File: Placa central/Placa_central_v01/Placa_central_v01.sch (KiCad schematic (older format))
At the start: 35 parts, among them SW1 SW_comando1

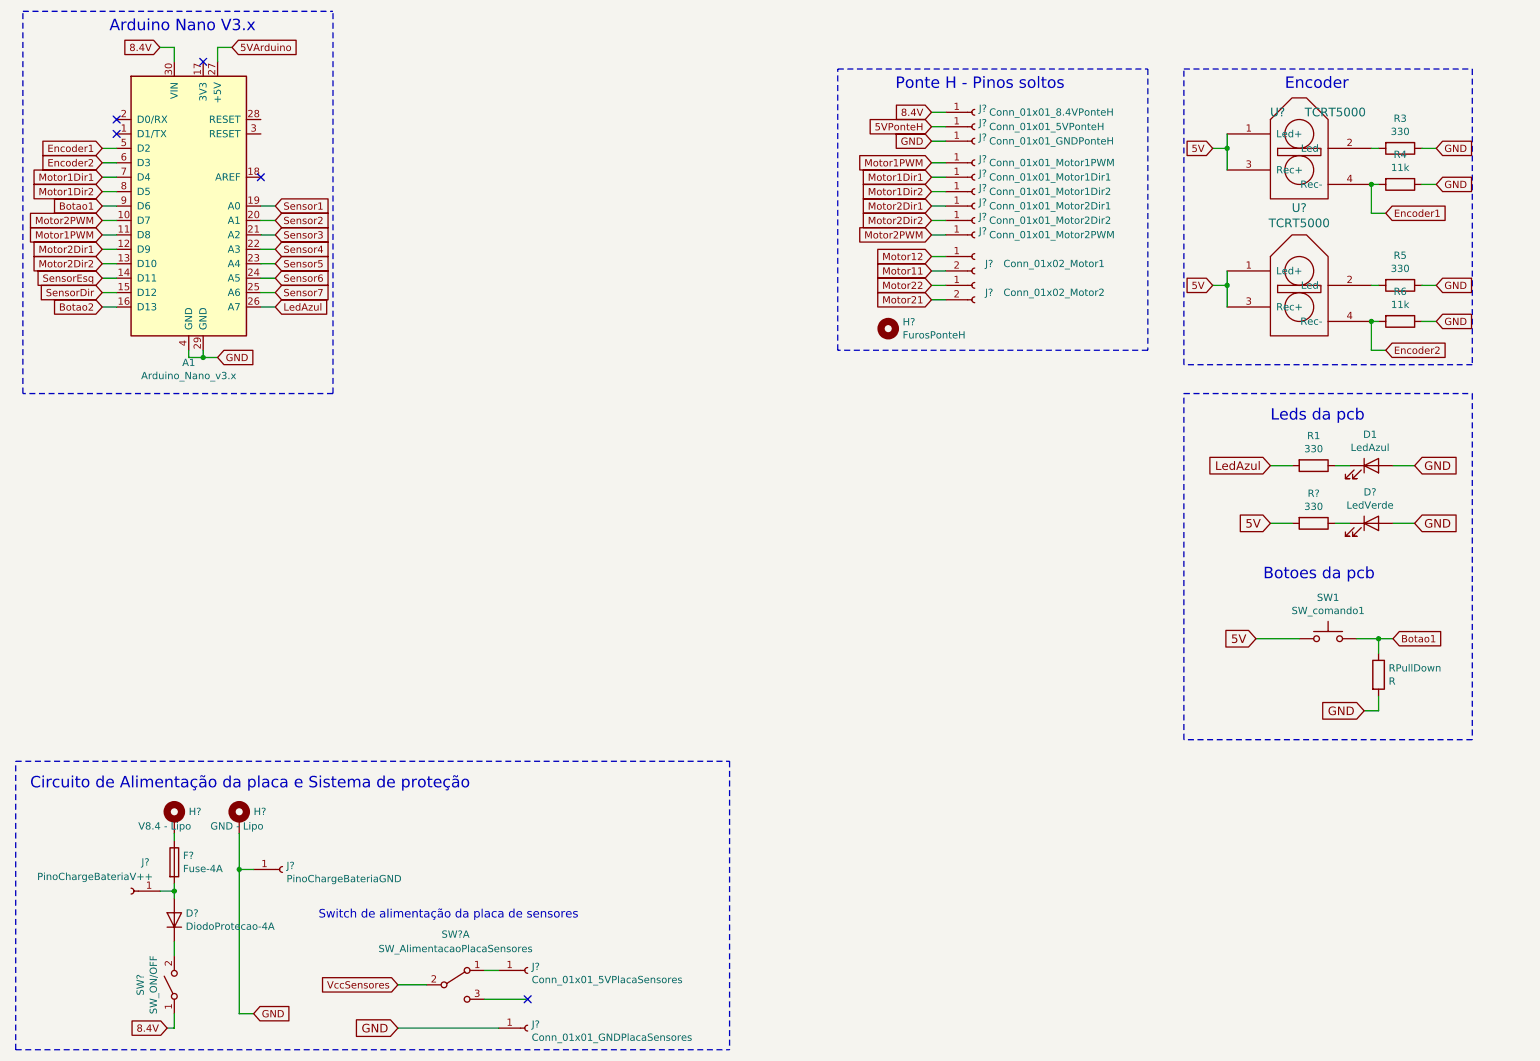
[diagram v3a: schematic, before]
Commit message: Terminado o esquemático do circuito
Feito: circuito medidor de bateria; pads do arduino; pads do encoder; pads da ponte H; pads da placa de sensores;
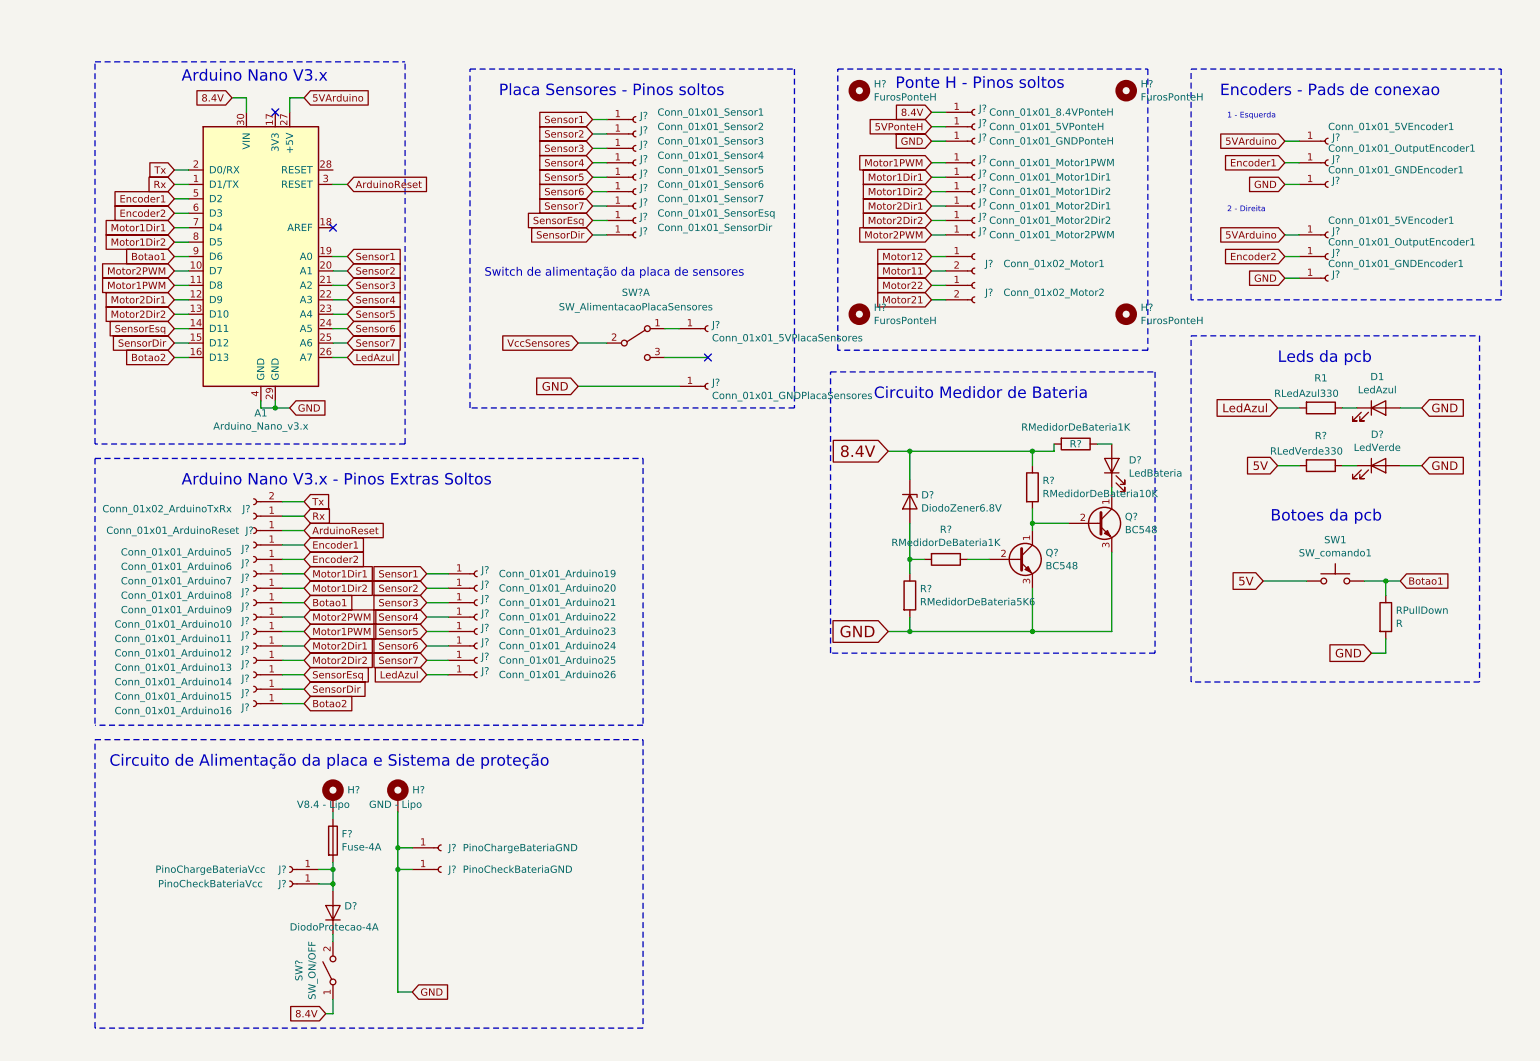
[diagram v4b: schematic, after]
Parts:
- removed R3, R5: 330, symbol Device:R
- removed R4, R6: 11k, symbol Device:R
- removed U? (x2): TCRT5000, symbol Sensores_e_componentes_SL:TCRT5000
- added D?: DiodoZener6.8V, symbol Device:D_Zener
- added D?: LedBateria, symbol Device:LED
- added H? (x3): FurosPonteH, symbol Mechanical:MountingHole
- added J? (x2): Conn_01x01_5VEncoder1, symbol Connector:Conn_01x01_Female
- added J? (x2): Conn_01x01_OutputEncoder1, symbol Connector:Conn_01x01_Female
- added J? (x2): Conn_01x01_GNDEncoder1, symbol Connector:Conn_01x01_Female
- added J?: Conn_01x01_Sensor1, symbol Connector:Conn_01x01_Female
- added J?: Conn_01x01_Sensor2, symbol Connector:Conn_01x01_Female
- added J?: Conn_01x01_Sensor3, symbol Connector:Conn_01x01_Female
- added J?: Conn_01x01_Sensor4, symbol Connector:Conn_01x01_Female
- added J?: Conn_01x01_Sensor5, symbol Connector:Conn_01x01_Female
- added J?: Conn_01x01_Sensor6, symbol Connector:Conn_01x01_Female
- added J?: Conn_01x01_Sensor7, symbol Connector:Conn_01x01_Female
- added J?: Conn_01x01_SensorEsq, symbol Connector:Conn_01x01_Female
- added J?: Conn_01x01_SensorDir, symbol Connector:Conn_01x01_Female
- added J?: PinoCheckBateriaGND, symbol Connector:Conn_01x01_Female
- added J?: PinoCheckBateriaVcc, symbol Connector:Conn_01x01_Female
- added J?: Conn_01x01_Arduino16, symbol Connector:Conn_01x01_Female
- added J?: Conn_01x01_Arduino15, symbol Connector:Conn_01x01_Female
- added J?: Conn_01x01_Arduino14, symbol Connector:Conn_01x01_Female
- added J?: Conn_01x01_Arduino13, symbol Connector:Conn_01x01_Female
- added J?: Conn_01x01_Arduino12, symbol Connector:Conn_01x01_Female
- added J?: Conn_01x01_Arduino11, symbol Connector:Conn_01x01_Female
- added J?: Conn_01x01_Arduino10, symbol Connector:Conn_01x01_Female
- added J?: Conn_01x01_Arduino9, symbol Connector:Conn_01x01_Female
- added J?: Conn_01x01_Arduino8, symbol Connector:Conn_01x01_Female
- added J?: Conn_01x01_Arduino7, symbol Connector:Conn_01x01_Female
- added J?: Conn_01x01_Arduino6, symbol Connector:Conn_01x01_Female
- added J?: Conn_01x01_Arduino5, symbol Connector:Conn_01x01_Female
- added J?: Conn_01x01_Arduino26, symbol Connector:Conn_01x01_Female
- added J?: Conn_01x01_Arduino25, symbol Connector:Conn_01x01_Female
- added J?: Conn_01x01_Arduino24, symbol Connector:Conn_01x01_Female
- added J?: Conn_01x01_Arduino23, symbol Connector:Conn_01x01_Female
- added J?: Conn_01x01_Arduino22, symbol Connector:Conn_01x01_Female
- added J?: Conn_01x01_Arduino21, symbol Connector:Conn_01x01_Female
- added J?: Conn_01x01_Arduino20, symbol Connector:Conn_01x01_Female
- added J?: Conn_01x01_Arduino19, symbol Connector:Conn_01x01_Female
- added J?: Conn_01x02_ArduinoTxRx, symbol Connector:Conn_01x02_Female
- added J?: Conn_01x01_ArduinoReset, symbol Connector:Conn_01x01_Female
- added Q? (x2): BC548, Package_TO_SOT_THT:TO-92_Inline, symbol Transistor_BJT:BC548
- added R? (x2): RMedidorDeBateria1K, symbol Device:R
- added R?: RMedidorDeBateria5K6, symbol Device:R
- added R?: RMedidorDeBateria10K, symbol Device:R
- J?: value PinoChargeBateriaV++ -> PinoChargeBateriaVcc
- R1: value 330 -> RLedAzul330
- R?: value 330 -> RLedVerde330
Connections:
- net 5VArduino: now also J?.1 (Pin_1), J?.1 (Pin_1)
- net 8.4V: now also D?.1 (K), R?.1, R?.2
- net Botao1: now also J?.1 (Pin_1)
- net Botao2: now also J?.1 (Pin_1)
- net Encoder1: now also J?.1 (Pin_1), J?.1 (Pin_1)
- net Encoder2: now also J?.1 (Pin_1), J?.1 (Pin_1)
- net GND: now also J?.1 (Pin_1), J?.1 (Pin_1), J?.1 (Pin_1), Q?.3 (E), Q?.3 (E), R?.2
- net LedAzul: now also J?.1 (Pin_1)
- net Motor1Dir1: now also J?.1 (Pin_1)
- net Motor1Dir2: now also J?.1 (Pin_1)
- net Motor1PWM: now also J?.1 (Pin_1)
- net Motor2Dir1: now also J?.1 (Pin_1)
- net Motor2Dir2: now also J?.1 (Pin_1)
- net Motor2PWM: now also J?.1 (Pin_1)
- net Sensor1: now also J?.1 (Pin_1), J?.1 (Pin_1)
- net Sensor2: now also J?.1 (Pin_1), J?.1 (Pin_1)
- net Sensor3: now also J?.1 (Pin_1), J?.1 (Pin_1)
- net Sensor4: now also J?.1 (Pin_1), J?.1 (Pin_1)
- net Sensor5: now also J?.1 (Pin_1), J?.1 (Pin_1)
- net Sensor6: now also J?.1 (Pin_1), J?.1 (Pin_1)
- net Sensor7: now also J?.1 (Pin_1), J?.1 (Pin_1)
- net SensorDir: now also J?.1 (Pin_1), J?.1 (Pin_1)
- net SensorEsq: now also J?.1 (Pin_1), J?.1 (Pin_1)
- net Rx: now reaches A1.1 (D1/TX)
- net Rx: now also J?.1 (Pin_1)
- net Tx: now reaches A1.2 (D0/RX)
- net Tx: now also J?.2 (Pin_2)
- net ArduinoReset: now reaches A1.3 (RESET)
- net ArduinoReset: now also J?.1 (Pin_1)
- net at D?.2 (A), F?.2, J?.1 (Pin_1): now also J?.1 (Pin_1)
- new net: D?.2 (A), R?.1, R?.2
- new net: Q?.2 (B), R?.1
- new net: Q?.1 (C), Q?.2 (B), R?.2
- new net: D?.2 (A), R?.1
- new net: D?.1 (K), Q?.1 (C)
- no-connect marks 5 -> 3
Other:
- note added: "1 - Esquerda\n"
- note added: "2 - Direita"
- note added: "Arduino Nano V3.x - Pinos Extras Soltos"
- note added: "Circuito Medidor de Bateria"
- note added: "Encoders - Pads de conexao"
- note added: "Placa Sensores - Pinos soltos"
- note removed: "Encoder"
- moved on the sheet: A1, D1, D?, F?, H?, J?, R1, R?, RPullDown, SW1, SW?, SW?A

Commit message: Acertada nomeclatura do encoder
De encoder1 para encoderEsq e a mesma coisa pro outro.
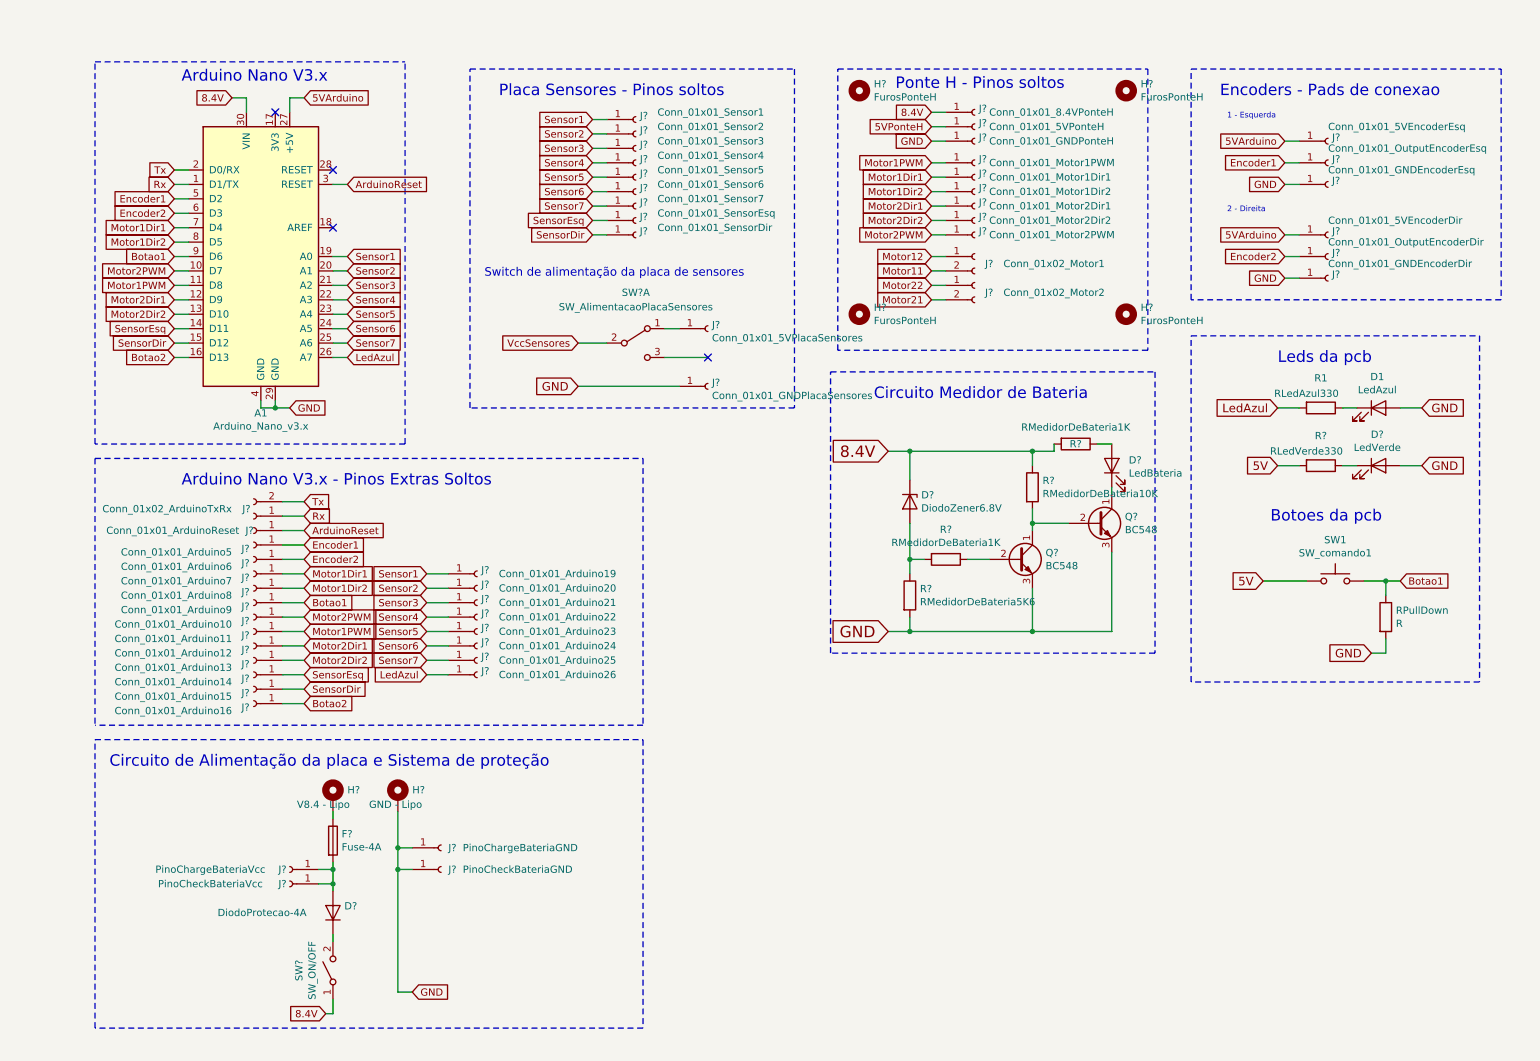
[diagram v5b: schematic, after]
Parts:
- J?: value Conn_01x01_5VEncoder1 -> Conn_01x01_5VEncoderEsq
- J?: value Conn_01x01_OutputEncoder1 -> Conn_01x01_OutputEncoderEsq
- J?: value Conn_01x01_GNDEncoder1 -> Conn_01x01_GNDEncoderEsq
- J?: value Conn_01x01_5VEncoder1 -> Conn_01x01_5VEncoderDir
- J?: value Conn_01x01_OutputEncoder1 -> Conn_01x01_OutputEncoderDir
- J?: value Conn_01x01_GNDEncoder1 -> Conn_01x01_GNDEncoderDir
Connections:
- no-connect marks 3 -> 4
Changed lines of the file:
@@
 P 2750 6800
 F 0 "D?" V 2796 6721 50  0000 R CNN
-F 1 "DiodoProtecao-4A" V 2650 7100 50  0000 R CNN
+F 1 "DiodoProtecao-4A" V 2750 7600 50  0000 R CNN
 F 2 "" H 2750 6800 50  0001 C CNN
 F 3 "~" H 2750 6800 50  0001 C CNN
@@
 P 9650 1450
 F 0 "J?" H 9678 1476 50  0000 L CNN
-F 1 "Conn_01x01_5VEncoder1" H 9650 1550 50  0000 L CNN
+F 1 "Conn_01x01_5VEncoderEsq" H 9650 1550 50  0000 L CNN
 F 2 "" H 9650 1450 50  0001 C CNN
 F 3 "~" H 9650 1450 50  0001 C CNN
@@
 P 9650 1600
 F 0 "J?" H 9678 1626 50  0000 L CNN
-F 1 "Conn_01x01_OutputEncoder1" H 9650 1700 50  0000 L CNN
+F 1 "Conn_01x01_OutputEncoderEsq" H 9650 1700 50  0000 L CNN
 F 2 "" H 9650 1600 50  0001 C CNN
 F 3 "~" H 9650 1600 50  0001 C CNN
@@
 P 9650 1750
 F 0 "J?" H 9677 1776 50  0000 L CNN
-F 1 "Conn_01x01_GNDEncoder1" H 9650 1850 50  0000 L CNN
+F 1 "Conn_01x01_GNDEncoderEsq" H 9650 1850 50  0000 L CNN
 F 2 "" H 9650 1750 50  0001 C CNN
 F 3 "~" H 9650 1750 50  0001 C CNN
@@
 P 9650 2100
 F 0 "J?" H 9678 2126 50  0000 L CNN
-F 1 "Conn_01x01_5VEncoder1" H 9650 2200 50  0000 L CNN
+F 1 "Conn_01x01_5VEncoderDir" H 9650 2200 50  0000 L CNN
 F 2 "" H 9650 2100 50  0001 C CNN
 F 3 "~" H 9650 2100 50  0001 C CNN
@@
 P 9650 2250
 F 0 "J?" H 9678 2276 50  0000 L CNN
-F 1 "Conn_01x01_OutputEncoder1" H 9650 2350 50  0000 L CNN
+F 1 "Conn_01x01_OutputEncoderDir" H 9650 2350 50  0000 L CNN
 F 2 "" H 9650 2250 50  0001 C CNN
 F 3 "~" H 9650 2250 50  0001 C CNN
@@
 P 9650 2400
 F 0 "J?" H 9677 2426 50  0000 L CNN
-F 1 "Conn_01x01_GNDEncoder1" H 9650 2500 50  0000 L CNN
+F 1 "Conn_01x01_GNDEncoderDir" H 9650 2500 50  0000 L CNN
 F 2 "" H 9650 2400 50  0001 C CNN
 F 3 "~" H 9650 2400 50  0001 C CNN
@@
 Wire Wire Line
 	2550 4150 2400 4150
+NoConn ~ 2750 1650
 $EndSCHEMATC

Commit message: Pequenas mudanças
Acertado nomeclatura de resistor; colocado um resistor no circuito de medição na tensão da bateria (separado do circuito de charga da bateria); gerado a lista de componentes (.csv)
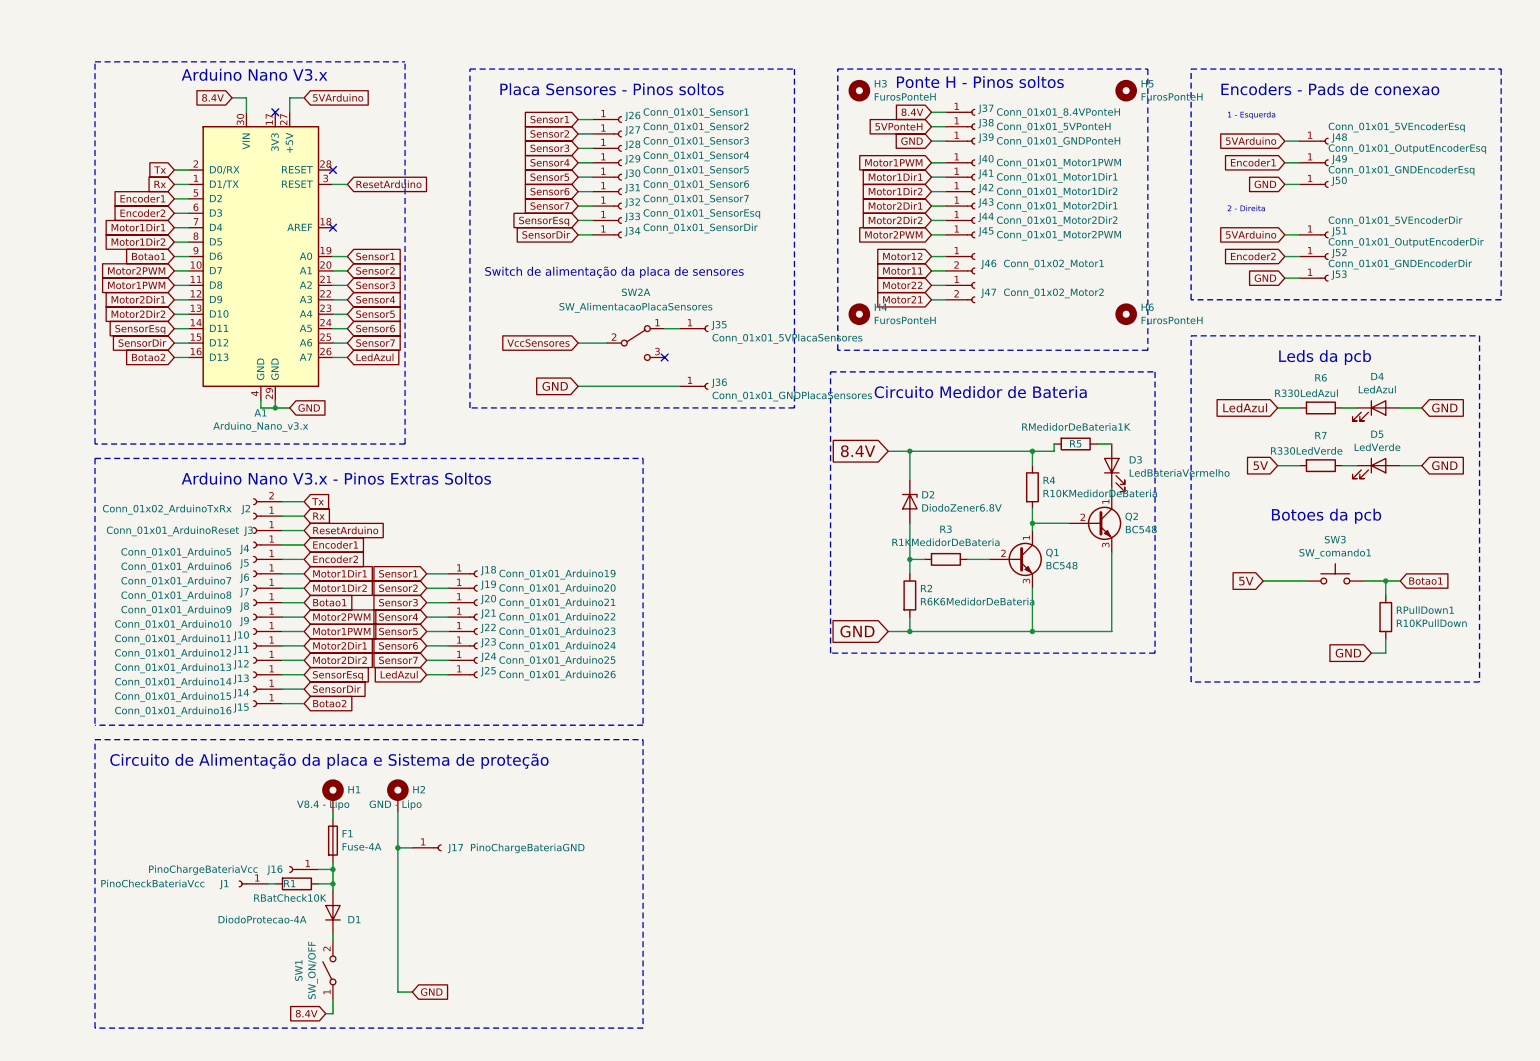
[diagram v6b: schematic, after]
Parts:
- removed J?: PinoCheckBateriaGND, symbol Connector:Conn_01x01_Female
- added R1: RBatCheck10K, symbol Device:R
- D3: renamed from D?; value LedBateria -> LedBateriaVermelho
- R2: renamed from R?; value RMedidorDeBateria5K6 -> R6K6MedidorDeBateria
- R3: renamed from R?; value RMedidorDeBateria1K -> R1KMedidorDeBateria
- R4: renamed from R?; value RMedidorDeBateria10K -> R10KMedidorDeBateria
- R6: renamed from R1; value RLedAzul330 -> R330LedAzul
- R7: renamed from R?; value RLedVerde330 -> R330LedVerde
- RPullDown1: renamed from RPullDown; value R -> R10KPullDown
- gave numbers to parts that had none: 68
- renumbered D1 to D4, SW1 to SW3
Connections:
- net at D1.2 (A), F1.2, J16.1 (Pin_1): now also R1.1; no longer J1.1 (Pin_1)
- net ArduinoReset renamed ResetArduino
- new net: J1.1 (Pin_1), R1.2
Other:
- moved on the sheet: J1, J26, J27, J28, J29, J30, J31, J32, J33, J34
